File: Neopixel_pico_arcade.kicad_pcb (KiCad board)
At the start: 4 copper layers, 100 x 100 mm, 147 parts, among them J1 SWD_connector, J2 NES_controller_connector, J3 USB_C_Receptacle_USB2.0, Q1 2N7002, U1 RP2040_Stamp, U2 SN74LV1T34DBV, U3 SRV05-4HTG-D

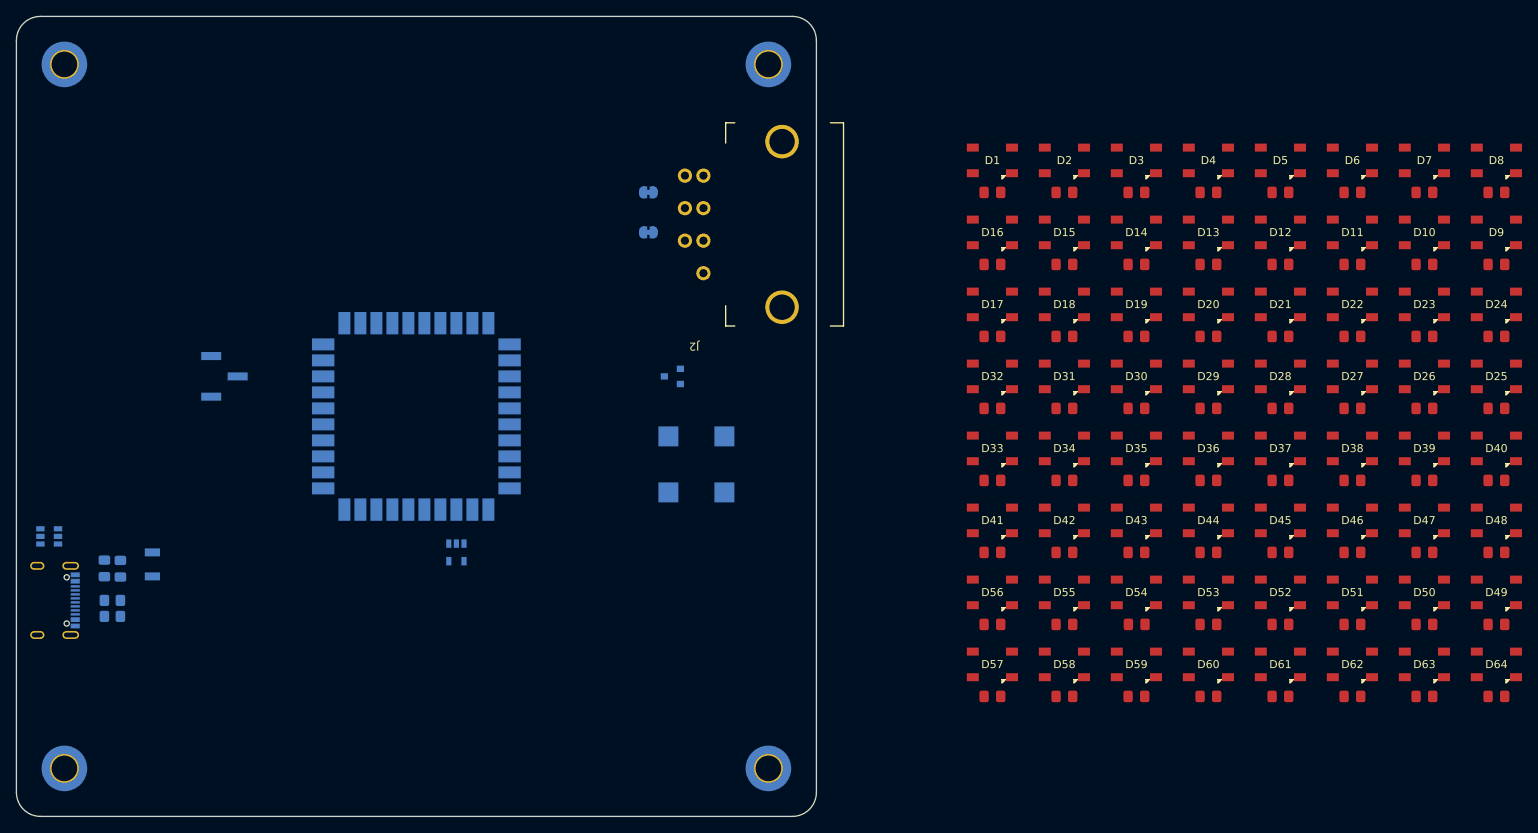
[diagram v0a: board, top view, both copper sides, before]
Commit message: Adjusts LED matrix placement
Because of the NES connector and it's through hole leads it's really
hard to keep it symmetric while keeping it under 100mm x 100mm*. The
solution I found is to keep the spacing between the LEDs and the edges
the same in all but the side where the connectors are. This would
probably be better in the bottom, but then the cables would have nowhere
to exit from.

When designing a 3D printed enclosure we can try to hide this asymmetry.

* Since this is a 4 layer board, JLCPC's engineering fee will spike
  after this size threshold.
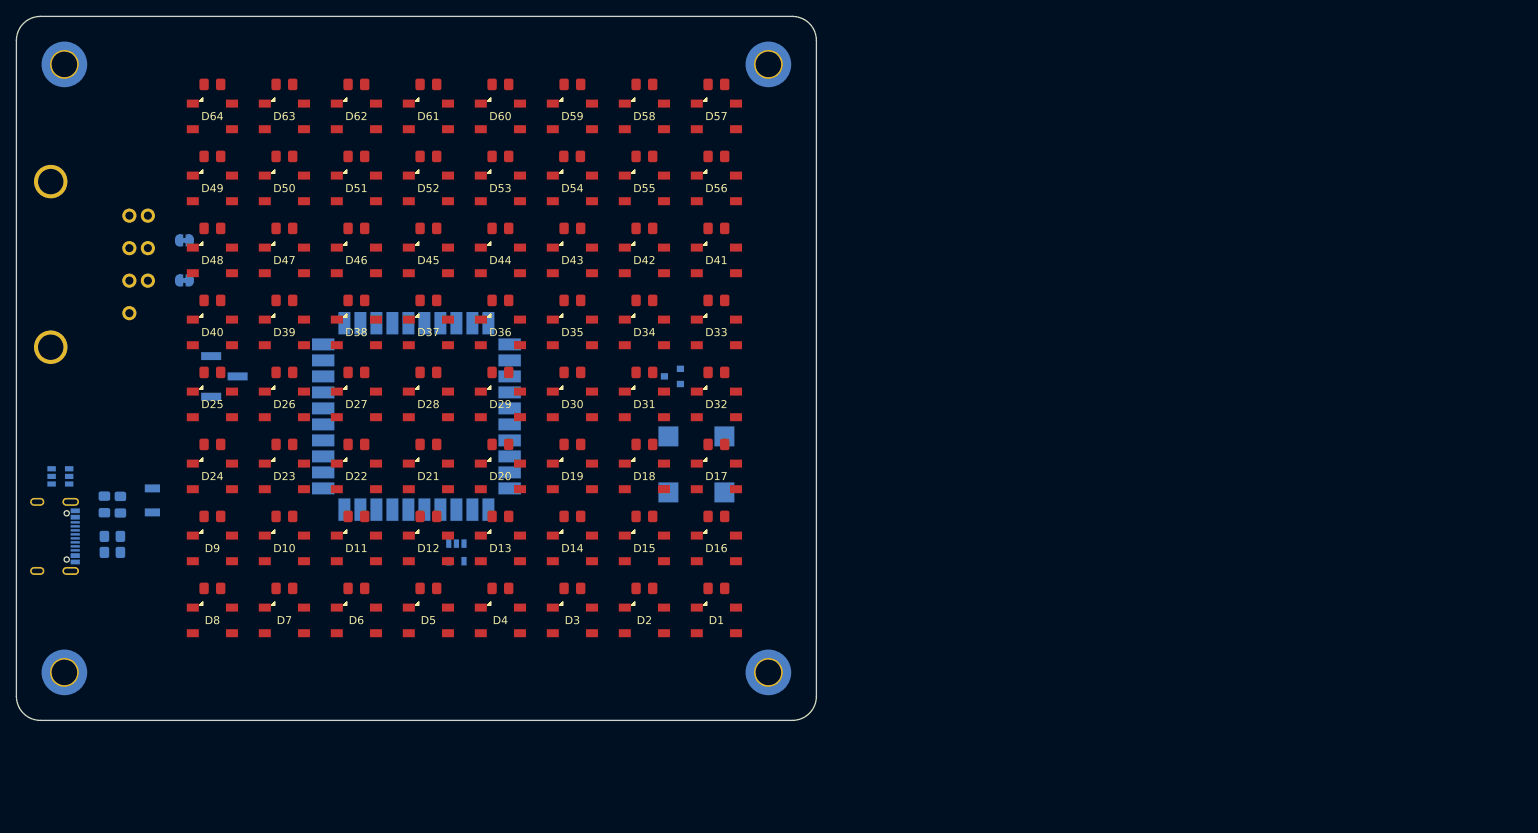
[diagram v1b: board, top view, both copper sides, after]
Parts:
- J2: moved to B.Cu
- moved C66 177.8 mm to (124.5, 58.5), turned to 180 degrees
- moved D64 174.5 mm to (124.5, 62.5), turned to 180 degrees
- moved C51 170.8 mm to (124.5, 67.5), turned to 180 degrees
- moved D8 170.5 mm to (124.5, 125.5), turned to 180 degrees
- moved D49 168.3 mm to (124.5, 71.5), turned to 180 degrees
- moved C10 168.0 mm to (124.5, 121.5), turned to 180 degrees
- moved C50 165.5 mm to (124.5, 76.5), turned to 180 degrees
- moved D9 165.3 mm to (124.5, 116.5), turned to 180 degrees
- moved D48 163.8 mm to (124.5, 80.5), turned to 180 degrees
- moved C11 163.6 mm to (124.5, 112.5), turned to 180 degrees
- moved C42 162.1 mm to (124.5, 85.5), turned to 180 degrees
- moved D24 161.9 mm to (124.5, 107.5), turned to 180 degrees
- moved C65 161.7 mm to (133.5, 58.5), turned to 180 degrees
- moved D40 161.2 mm to (124.5, 89.5), turned to 180 degrees
- moved C26 161.1 mm to (124.5, 103.5), turned to 180 degrees
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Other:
- board size 100 x 100 mm -> 100 x 88 mm

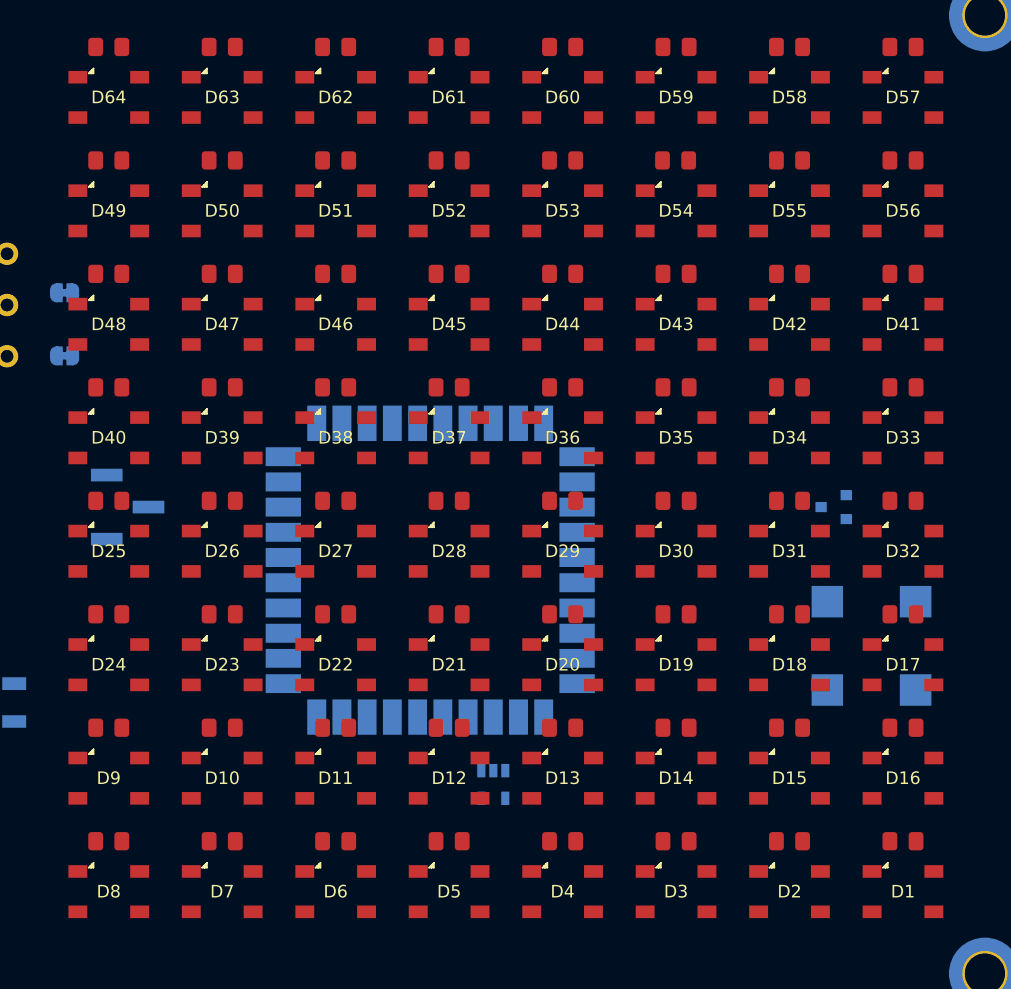
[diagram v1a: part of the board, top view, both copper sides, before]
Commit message: Fixes LED ordering in the matrix
After routing some of the LED data pins, I noticed some of the last rows
were wrong.
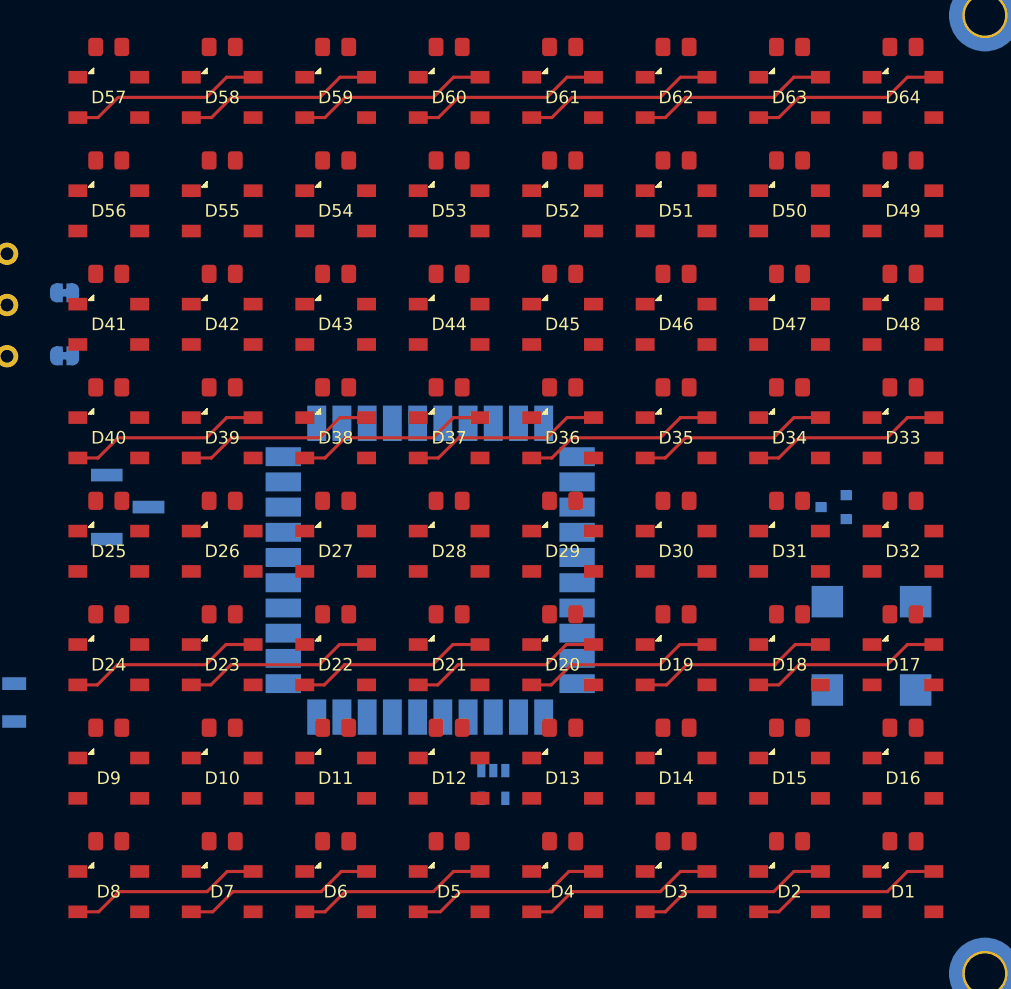
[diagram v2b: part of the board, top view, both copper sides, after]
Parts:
- moved C43 63.0 mm to (124.5, 76.5)
- moved C50 63.0 mm to (187.5, 76.5)
- moved C51 63.0 mm to (187.5, 67.5)
- moved C58 63.0 mm to (124.5, 67.5)
- moved C59 63.0 mm to (124.5, 58.5)
- moved C66 63.0 mm to (187.5, 58.5)
- moved D41 63.0 mm to (124.5, 80.5)
- moved D48 63.0 mm to (187.5, 80.5)
- moved D49 63.0 mm to (187.5, 71.5)
- moved D56 63.0 mm to (124.5, 71.5)
- moved D57 63.0 mm to (124.5, 62.5)
- moved D64 63.0 mm to (187.5, 62.5)
- moved C44 45.0 mm to (133.5, 76.5)
- moved C49 45.0 mm to (178.5, 76.5)
- moved C52 45.0 mm to (178.5, 67.5)
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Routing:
- net Net-(D7-Pad2): track 0.00 -> 15.2 mm
- net Net-(D6-Pad2): track 0.00 -> 15.2 mm
- net Net-(D4-Pad2): track 0.00 -> 15.2 mm
- net Net-(D18-Pad2): track 0.00 -> 15.2 mm
- net Net-(D63-Pad2): track 0.00 -> 15.2 mm
- net Net-(D22-Pad2): track 0.00 -> 15.2 mm
- net Net-(D21-Pad2): track 0.00 -> 15.2 mm
- net Net-(D20-Pad2): track 0.00 -> 15.2 mm
- net Net-(D19-Pad2): track 0.00 -> 15.2 mm
- net Net-(D23-Pad2): track 0.00 -> 15.2 mm
- net Net-(D39-Pad2): track 0.00 -> 15.2 mm
- net Net-(D62-Pad2): track 0.00 -> 15.2 mm
- net Net-(D61-Pad2): track 0.00 -> 15.2 mm
- net Net-(D60-Pad2): track 0.00 -> 15.2 mm
- net Net-(D59-Pad2): track 0.00 -> 15.2 mm
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
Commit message: Routes data pins between the LEDs
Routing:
- net Net-(D54-Pad2): track 0.00 -> 15.2 mm
- net Net-(D53-Pad2): track 0.00 -> 15.2 mm
- net Net-(D52-Pad2): track 0.00 -> 15.2 mm
- net Net-(D55-Pad2): track 0.00 -> 15.2 mm
- net Net-(D51-Pad2): track 0.00 -> 15.2 mm
- net Net-(D50-Pad2): track 0.00 -> 15.2 mm
- net Net-(D49-Pad2): track 0.00 -> 15.2 mm
- net Net-(D8-Pad2): track 0.00 -> 9.35 mm
- net Net-(D56-Pad2): track 0.00 -> 9.35 mm
- net Net-(D40-Pad2): track 0.00 -> 9.35 mm
- net Net-(D24-Pad2): track 0.00 -> 9.35 mm
- net Net-(D48-Pad2): track 0.00 -> 9.35 mm
- net Net-(D32-Pad2): track 0.00 -> 9.35 mm
- net Net-(D16-Pad2): track 0.00 -> 9.35 mm
- net Net-(D57-Pad2): track 15.2 -> 6.60 mm
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
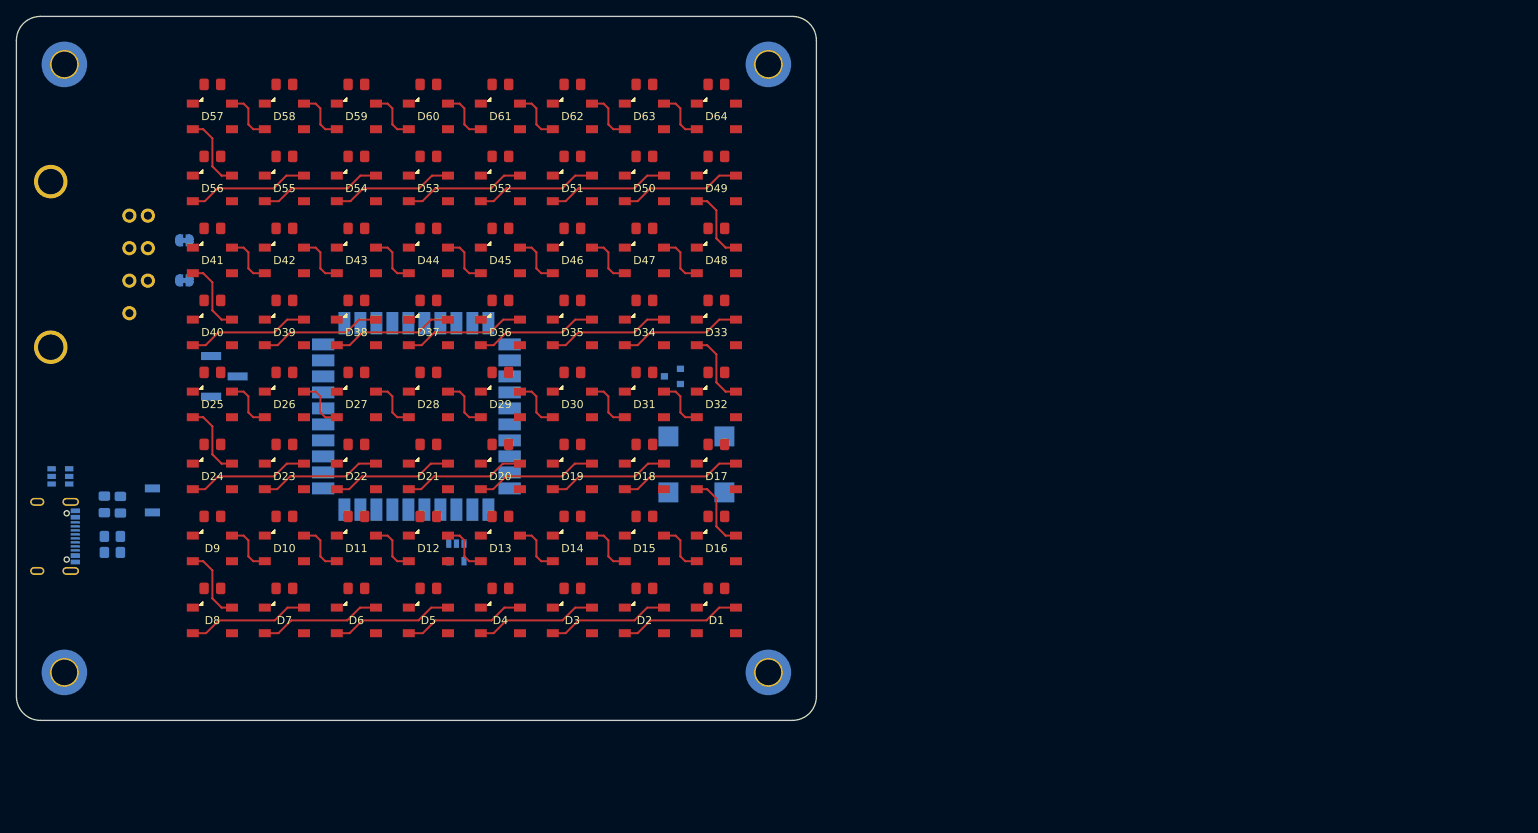
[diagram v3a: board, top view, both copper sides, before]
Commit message: First rough pass at routing
Everything can be improved a lot, and I don't have vias to ground on the
top layer. The 3v3 line to the controller is also missing.
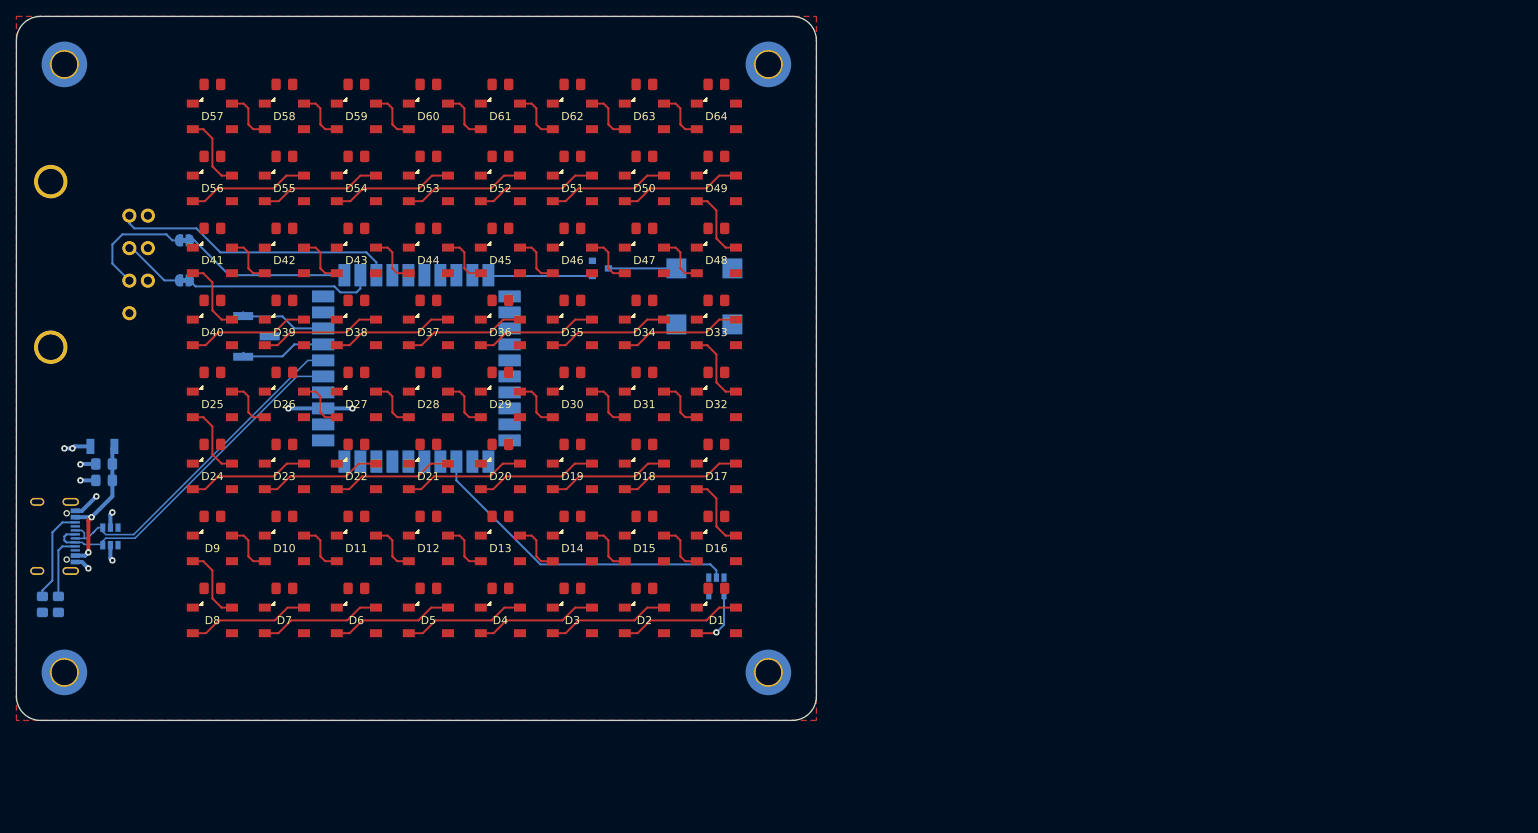
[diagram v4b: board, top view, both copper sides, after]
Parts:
- moved U2 32.8 mm to (187.5, 121.2)
- moved BZ1 21.0 mm to (186.0, 85.0)
- moved Q1 16.2 mm to (173.0, 81.5), turned to 0 degrees
- moved R2 12.2 mm to (103.2, 123.5), turned to -90 degrees
- moved U3 9.76 mm to (111.8, 115.0), turned to 90 degrees
- moved R1 9.37 mm to (105.2, 123.5), turned to -90 degrees
- moved F1 9.20 mm to (110.8, 103.8), turned to 180 degrees
- moved J1 6.40 mm to (130.0, 90.0)
- moved U1 6.00 mm to (150.0, 94.0)
- moved C2 5.05 mm to (111.0, 106.0), turned to 180 degrees
- moved C1 3.66 mm to (111.0, 108.0), turned to 180 degrees
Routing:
- net USB_D+: track 0.00 -> 43.6 mm
- net USB_D-: track 0.00 -> 43.6 mm
- net Net-(U1-Pad23): track 0.00 -> 40.4 mm
- net CTRL_DATA: track 0.00 -> 35.5 mm
- net CTRL_LATCH: track 0.00 -> 23.8 mm
- net CTRL_CLK: track 0.00 -> 21.2 mm
- net Net-(C1-Pad1): track 0.00 -> 18.4 mm, vias 0 -> 2
- net Net-(J2-Pad2): track 0.00 -> 14.6 mm
- net +5V: track 0.00 -> 13.4 mm, vias 0 -> 5
- net BUZZ: track 0.00 -> 13.0 mm
- net Net-(J3-PadB5): track 0.00 -> 11.9 mm
- net GND: track 0.00 -> 11.2 mm, vias 0 -> 5
- net SWCLK: track 0.00 -> 10.8 mm
- net SWDIO: track 0.00 -> 10.8 mm
- net Net-(BZ1-Pad2): track 0.00 -> 8.50 mm
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- added copper zone on F.Cu, net +5V
- added copper zone on In1.Cu, net GND
- added copper zone on In2.Cu, net GND
